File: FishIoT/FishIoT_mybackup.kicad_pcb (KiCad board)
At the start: 4 copper layers, 42 x 70 mm, 117 parts, among them IC1 RV-3032-C7_32.768KHZ-2.5PPM-T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, J1 USB4105-GF-A-120, J3 Conn_Coaxial, J4 BM05B-ZESS-TBT, J5 SF72S006VBDR2500, J6 Conn_Coaxial, J7 SHF-105-01-L-D-SM, J8 0705430001, SW1 PTS645SM43SMTR92 LF, SW2 PTS645SM43SMTR92 LF, SW3 PTS645SM43SMTR92 LF, U1 USBLC6-2P6, U2 NRF9151-LACA-R7, U3 CP2102N-Axx-xQFN20, U4 MAX-M10S, U5 TPD3F303DPVR, U6 MAX3471, U7 SI1040X-T1-GE3, U8 TPS63000

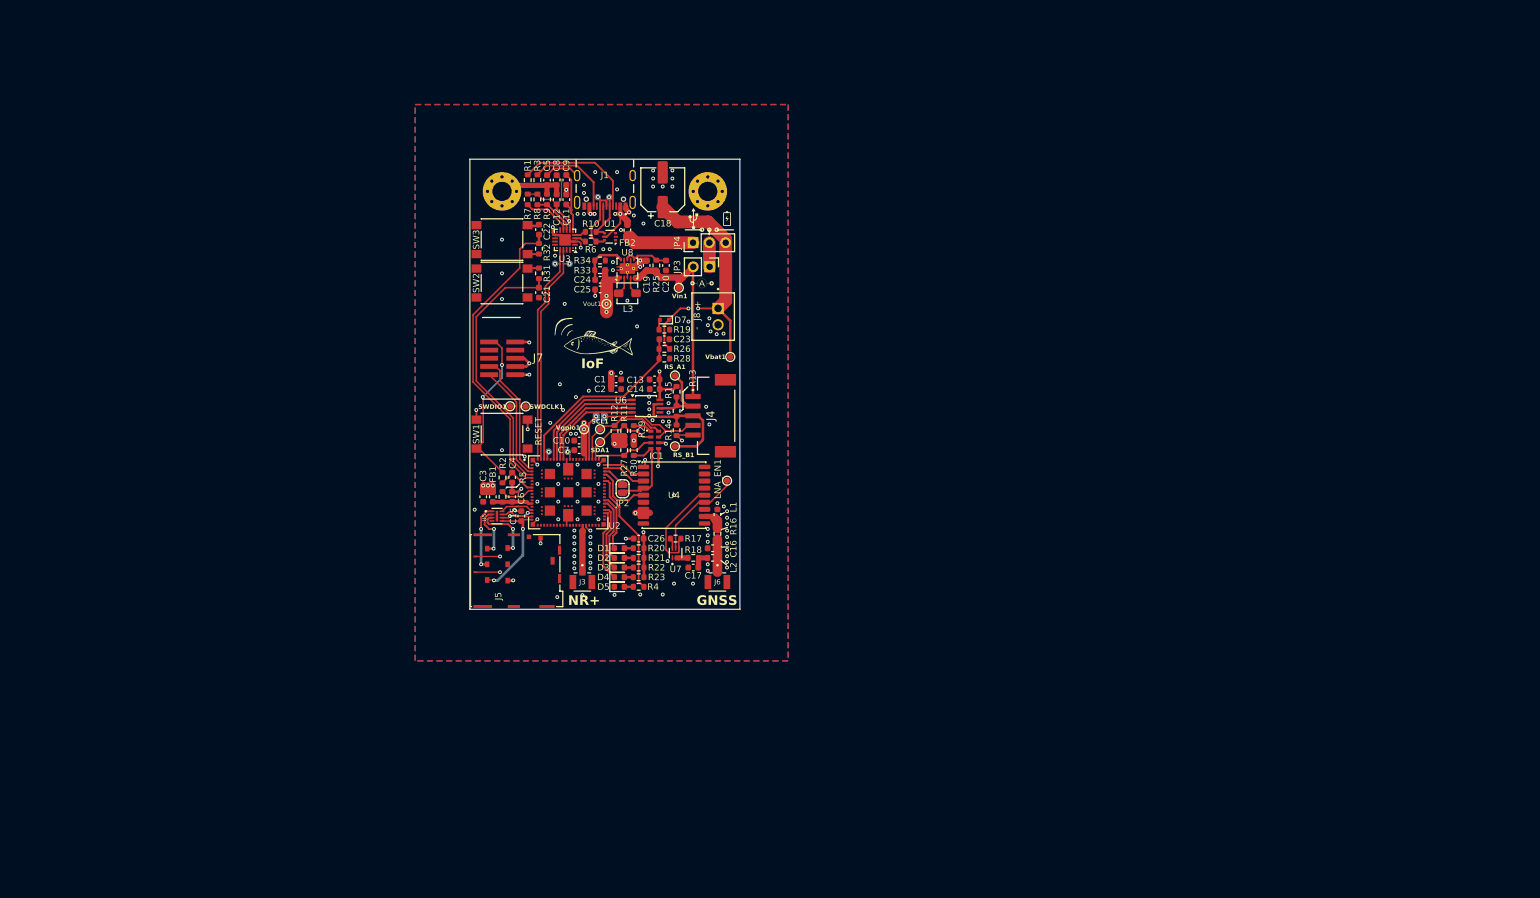
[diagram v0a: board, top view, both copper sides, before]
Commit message: v26.0
First draft of schematics and PCB with nRF9151
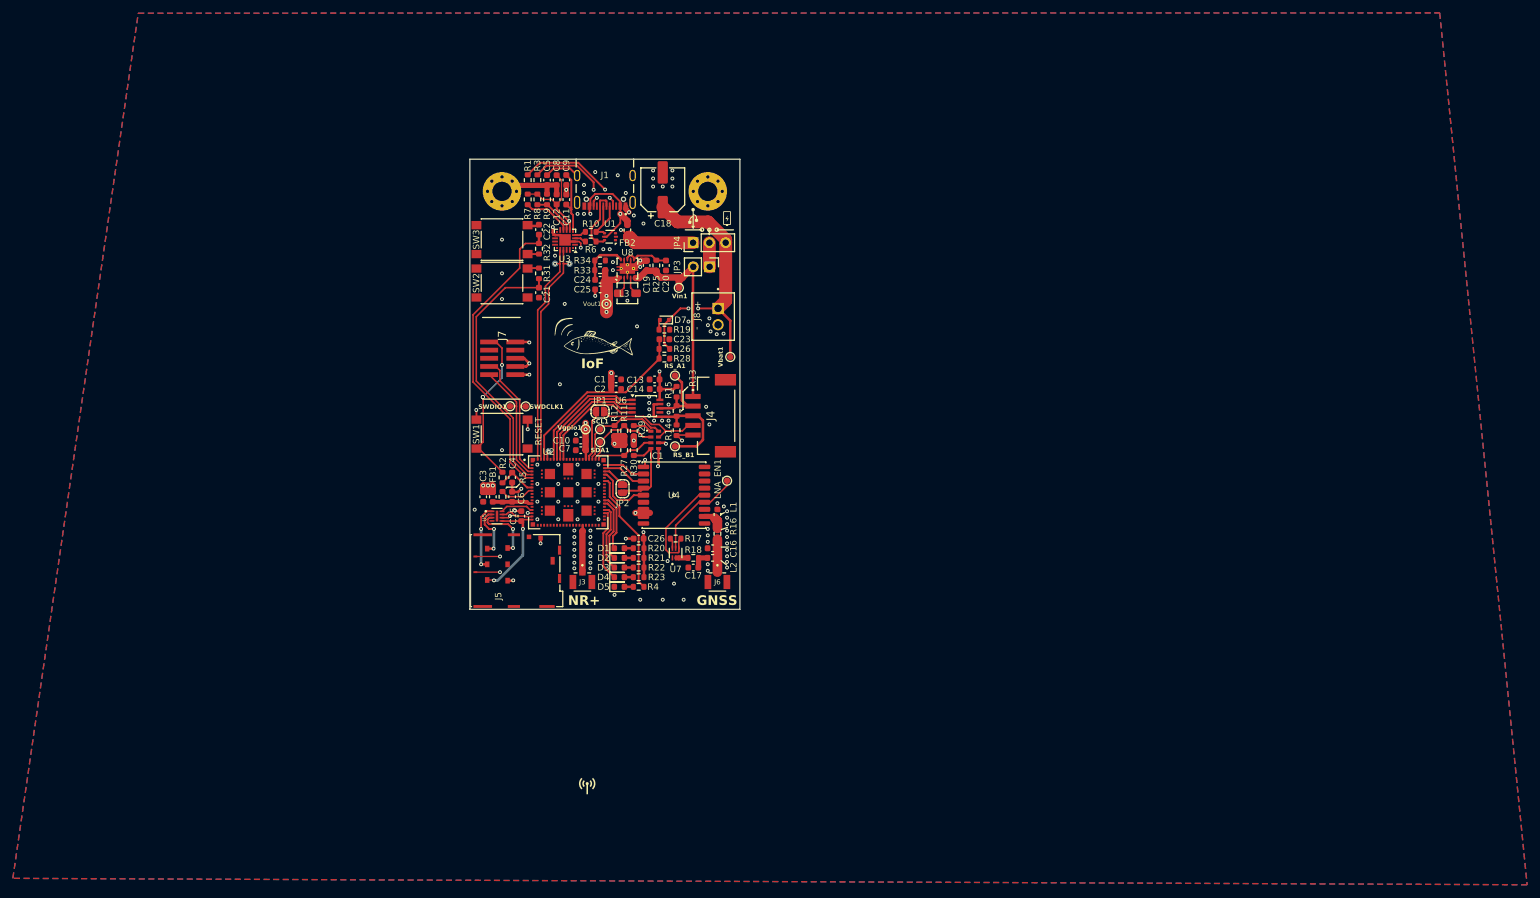
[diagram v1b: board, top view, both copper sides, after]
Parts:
- removed D+1, D-1, GPIO_0.11: TestPoint, TestPoint:TestPoint_Pad_D1.0mm
- added G***: LOGO, FishIoT_Footprint_library:antennalogo, F.Cu at (110.8, 126.5)
- G***: moved to B.Cu
- JP1: moved to F.Cu
- moved G*** 11.0 mm to (139.0, 44.7), turned to 180 degrees
- moved JP1 0.75 mm to (112.8, 68.2)
- moved C10 0.25 mm to (109.8, 72.8)
- moved C7 0.25 mm to (109.8, 74.2)
- moved Vgpio1 0.25 mm to (110.5, 71.0)
- turned G*** to 180 degrees (x2)
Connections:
- U2 pad 70: Net-(U2A-P0.11) -> unconnected-(U2A-P0.11-Pad70)
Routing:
- net GND: track 72.8 -> 65.0 mm, vias 133 -> 124
- net /VUSB_C: track 14.1 -> 21.5 mm, vias 4 -> 2
- net /D-: track 10.8 -> 9.19 mm, vias 1 -> 0
- net Net-(J1-CC1): track 19.1 -> 17.7 mm, vias 0 -> 2
- net Net-(U2A-P0.11): track 1.32 -> 0.00 mm, vias 1 -> 0
- net /RS485_DI: track 15.9 -> 16.9 mm
- net /RS485_DE: track 16.8 -> 17.6 mm
- net Net-(JP1-A): track 7.12 -> 7.86 mm, vias 1 -> 0
- net /D+: track 11.1 -> 10.5 mm, vias 1 -> 0
- net /RS485_RE: track 17.7 -> 18.4 mm
- net Net-(J1-CC2): track 14.1 -> 14.5 mm, vias 0 -> 2
- net /RTC_CLKOUT: track 16.5 -> 16.9 mm, vias 1 -> 0
- net /~{nRESET}: vias 2 -> 3
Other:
- board text removed: "D+"
- board text removed: "D-"
- board text removed: "github.com/autoHammer/IoF-v26-Design-Files"
